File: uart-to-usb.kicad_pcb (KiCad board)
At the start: 2 copper layers, 37 x 14 mm, 11 parts, among them J1 USB_C_Receptacle_USB2.0_16P, J2 Conn_01x02_Pin, U1 FT232RL

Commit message: Add part for BOM
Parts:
- R1, R2: footprint Resistor_SMD:R_0805_2012Metric -> Resistor_SMD:R_0603_1608Metric
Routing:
- net Net-(C4-Pad1): track 6.07 -> 12.6 mm
- net +5V: track 14.6 -> 16.5 mm
- removed copper zone on B.Cu, net GND

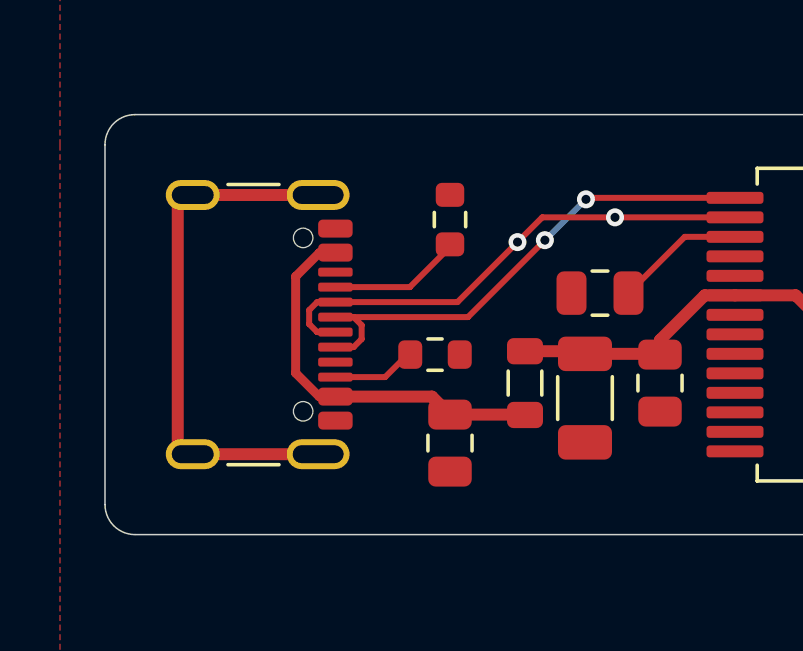
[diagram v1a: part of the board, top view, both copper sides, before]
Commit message: Fix usb-c alignment
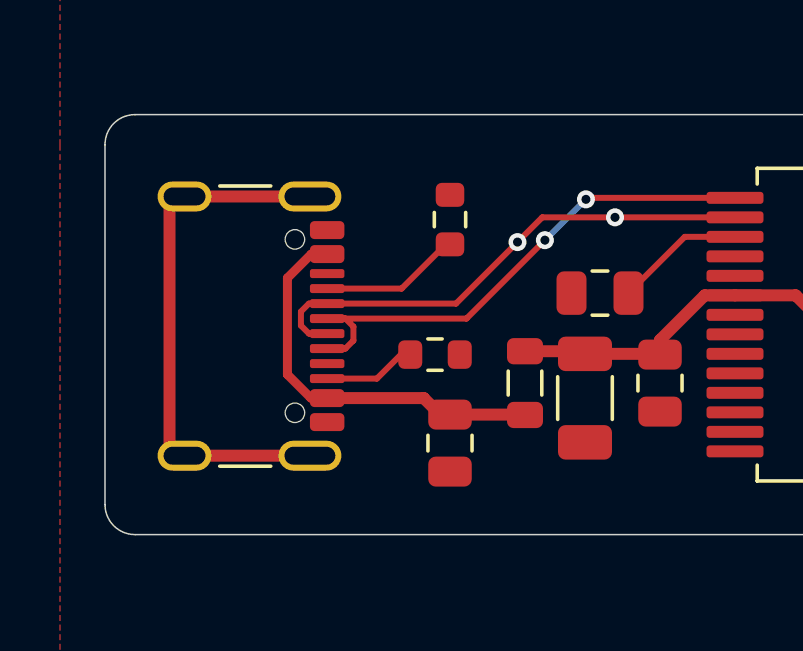
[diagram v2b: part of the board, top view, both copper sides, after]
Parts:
- moved J1 0.28 mm to (127.2, 96.5)
